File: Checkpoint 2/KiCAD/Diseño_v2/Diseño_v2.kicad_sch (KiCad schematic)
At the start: 40 parts, among them J1 Conn_01x02, J2 Conn_01x02, J3 Conn_01x03, Q1 BC547, Q2 BC547, Q3 BC557, Q4 BC557, Q5 BC547, Q6 TIP32A, Q7 BC547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

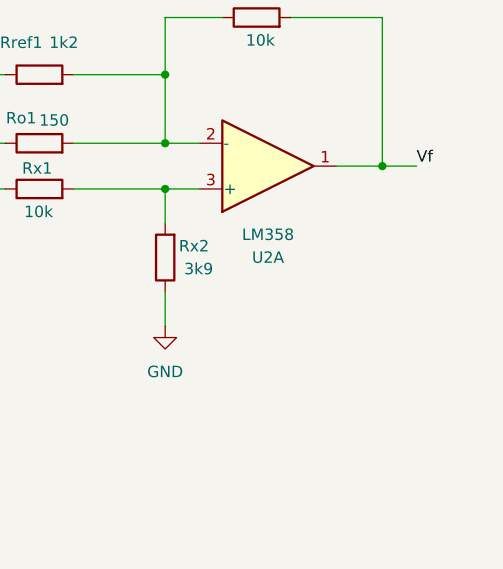
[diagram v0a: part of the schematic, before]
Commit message: Corregí el esquemático y generé los archivos de fabricación
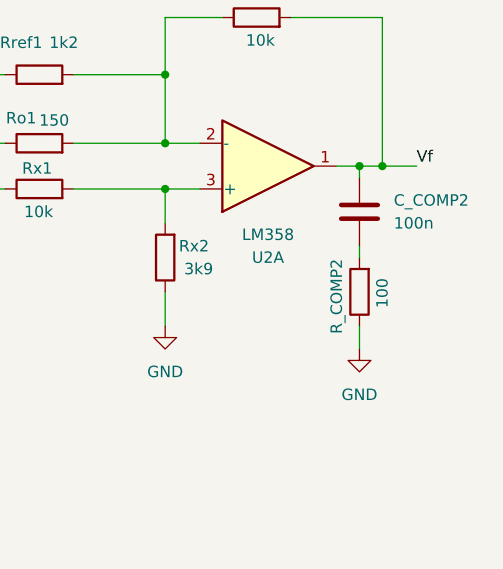
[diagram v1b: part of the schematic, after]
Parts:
- added C_COMP2: 100n, Capacitor_THT:C_Disc_D5.0mm_W2.5mm_P2.50mm, symbol Device:C
- added R_COMP2: 100, Resistor_THT:R_Axial_DIN0207_L6.3mm_D2.5mm_P7.62mm_Horizontal, symbol Device:R
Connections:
- net GND: now also R_COMP2.1
- net Vf: now also C_COMP2.2
- new net: C_COMP2.1, R_COMP2.2

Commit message: Actualicé el PCB
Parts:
- removed C_COMP2: 100n, Capacitor_THT:C_Disc_D5.0mm_W2.5mm_P2.50mm, symbol Device:C
- removed R_COMP2: 100, Resistor_THT:R_Axial_DIN0207_L6.3mm_D2.5mm_P7.62mm_Horizontal, symbol Device:R
- C_COMP1: value 68n -> 330n
- R_COMP1: value 100 -> 22
